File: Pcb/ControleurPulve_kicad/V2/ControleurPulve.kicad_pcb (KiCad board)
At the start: 2 copper layers, 92 parts, among them J1 Screw_Terminal_01x02, J10 Screw_Terminal_01x04, J11 Screw_Terminal_01x04, J12 Conn_01x03_Pin, J13 Conn_01x03_Pin, J14 Conn_01x03_Pin, J15 Conn_01x03_Pin, J16 Screw_Terminal_01x04, J17 Screw_Terminal_01x04, J18 Conn_01x03_Pin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

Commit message: PCB : silkscreen et placement (non routé)
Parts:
- added H5: e, MountingHole:MountingHole_3.2mm_M3, F.Cu at (131.1, 67.1)
- added H6: e, MountingHole:MountingHole_3.2mm_M3, F.Cu at (163.2, 88.4)
- added H7: e, MountingHole:MountingHole_3.2mm_M3, F.Cu at (131.1, 88.4)
- added R23: 2k5, Resistor_SMD:R_0603_1608Metric, F.Cu at (112.4, 88.6)
- added U9: ~, DIY_Modules:GY-NEO6MV2_25_36, F.Cu at (147.2, 77.7)
- G*** (x3): moved to B.Cu
- H4: value ~ -> e; footprint MountingHole:MountingHole_4.3mm_M4_DIN965_Pad_TopBottom -> MountingHole:MountingHole_3.2mm_M3
- J1: footprint TerminalBlock_RND:TerminalBlock_RND_205-00287_1x02_P5.08mm_Horizontal -> TerminalBlock_Phoenix:TerminalBlock_Phoenix_MKDS-1,5-2-5.08_1x02_P5.08mm_Horizontal
- J7: footprint Connector_PinSocket_2.54mm:PinSocket_1x06_P2.54mm_Vertical -> Connector_JST:JST_XH_B6B-XH-A_1x06_P2.50mm_Vertical
- R4: footprint Resistor_SMD:R_1206_3216Metric -> Resistor_SMD:R_0805_2012Metric
- moved G*** 269.1 mm to (180.8, 104.6), turned to 180 degrees
- moved G*** 225.5 mm to (151.6, 104.6), turned to 180 degrees
- moved TP3 185.4 mm to (105.5, 49.7)
- moved TP4 185.4 mm to (105.5, 53.2)
- moved TP5 185.4 mm to (105.5, 56.6)
- moved G*** 180.9 mm to (117.9, 104.1), turned to 180 degrees
- moved H1 168.4 mm to (91.0, 95.0)
- moved H4 118.7 mm to (163.2, 67.1)
- moved H3 108.0 mm to (170.0, 80.0)
- moved C4 86.6 mm to (112.2, 72.0)
- moved U1 81.8 mm to (120.5, 84.1)
- moved R1 80.3 mm to (139.6, 87.0), turned to -90 degrees
- moved R3 80.3 mm to (112.3, 86.6), turned to 180 degrees
- moved H2 79.0 mm to (191.0, 95.0)
- moved R2 74.5 mm to (137.0, 87.0), turned to -90 degrees
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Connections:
- J19 pad 2: Net-(J19-Pin_1) -> Net-(J19-Pin_2)
- J19 pad 3: Net-(J19-Pin_1) -> Net-(J19-Pin_3)
- JP5 pad 1: GND -> Net-(JP5-A)
- JP7 pad 1: GND -> Net-(JP5-A)
- R18 pad 1: Net-(J19-Pin_1) -> Net-(J19-Pin_2)
- R22 pad 2: Net-(J19-Pin_1) -> Net-(J19-Pin_3)
- U3 pad 3: unconnected-(U3-DEN-Pad3) -> Net-(U3-DEN)
- U4 pad 1: GND -> Net-(JP5-A)
- U8 pad 2: Net-(J19-Pin_1) -> Net-(J19-Pin_2)
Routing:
- added copper zone on B.Cu, net (none)
- added copper zone on F.Cu, net (none)
- added copper zone on In2.Cu, net (none)
- removed copper zone on B.Cu, net GND
- removed copper zone on F.Cu, net GND
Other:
- board outline added: 111.8 x 59.1 mm
- copper layers 2 -> 4
- board text added: "0-3V3"
- board text added: "0x49"
- board text added: "0x4A"
- board text added: "2025-10"
- board text added: "4-20 mA"
- board text added: "Ana"
- board text added: "Cl"
- board text added: "DG"
- board text added: "DM1-G"
- board text added: "DM2-cG"
- board text added: "DM3-cD"
- board text added: "DM4-D"
- board text added: "Da"
- board text added: "Débitdouille V2.0"
- board text added: "ESP32-C6 Xiao supermini"
- board text added: "Freq"
- board text added: "Gnd"
- board text added: "PRESS."
- board text added: "PWR"
- board text added: "Rx"
- board text added: "S"
- board text added: "Tx"
- board text added: "Vcc"
- board text added: "bypass 12Vout"
- board text added: "debit 4-20"
- board text added: "npn"
- board text added: "pnp"
- board text added: "press."
- board text removed: "DATA"
- board text removed: "Débitdouille V1.0"
- board text removed: "ESP32"
- board text removed: "PRESSION"
- board text removed: "RXD"
- board text removed: "TXD"

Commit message: Mise en prod
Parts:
- added D5: red, LED_SMD:LED_0603_1608Metric_Pad1.05x0.95mm_HandSolder, F.Cu at (109.0, 66.3)
- added FID1: Fiducial, Fiducial:Fiducial_0.5mm_Mask1.5mm, F.Cu at (87.0, 122.0)
- added FID2: Fiducial, Fiducial:Fiducial_0.5mm_Mask1.5mm, F.Cu at (195.0, 122.0)
- added FID3: Fiducial, Fiducial:Fiducial_0.5mm_Mask1.5mm, F.Cu at (87.0, 67.0)
- added G***: LOGO, LOGO, B.Cu at (93.2, 104.5)
- added R24: 2.2k, Resistor_SMD:R_0603_1608Metric_Pad0.98x0.95mm_HandSolder, F.Cu at (109.5, 68.9)
- C3: value 10uF -> 10uF X5R
- C5: value C -> 100nF
- C6: value C -> 10uF X5R
- C8: footprint Capacitor_SMD:C_0805_2012Metric -> Capacitor_SMD:C_0603_1608Metric
- D3: value LED -> green
- D4: value LED -> blue
- H1, H2, H3: footprint MountingHole:MountingHole_4.3mm_M4_DIN965_Pad_TopBottom -> MountingHole:MountingHole_3.2mm_M3_DIN965_Pad
- JP1: footprint Jumper:SolderJumper-2_P1.3mm_Open_TrianglePad1.0x1.5mm -> Jumper:SolderJumper-2_P1.3mm_Open_RoundedPad1.0x1.5mm; moved to B.Cu
- JP2, JP4, JP5, JP6, JP7: moved to B.Cu
- R4: value 150R .5% -> 150R .1%
- U5, U6, U7, U8: footprint Package_DIP:DIP-4_W7.62mm_SMDSocket_SmallPads -> Package_DIP:DIP-4_W8.89mm_SMDSocket_LongPads
- moved TP3 104.2 mm to (194.1, 104.7)
- moved TP4 98.1 mm to (191.2, 101.1)
- moved TP5 75.3 mm to (177.6, 78.5)
- moved R1 12.1 mm to (131.1, 95.5), turned to 90 degrees
- moved C3 10.8 mm to (112.4, 93.6), turned to 90 degrees
- moved JP1 9.42 mm to (110.2, 96.5)
- moved R2 9.20 mm to (133.6, 95.5), turned to 90 degrees
- moved H3 3.80 mm to (170.0, 76.2)
- moved JP4 3.27 mm to (122.7, 74.0), turned to 0 degrees
- moved R14 3.27 mm to (111.3, 68.9), turned to 90 degrees
- moved C11 3.02 mm to (172.7, 83.2)
- moved C10 2.39 mm to (172.7, 87.6)
- moved C9 2.39 mm to (172.7, 85.7)
- moved R23 2.34 mm to (112.4, 86.3)
- moved G*** 1.93 mm to (182.8, 104.8)
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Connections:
- U2 pad 1: unconnected-(U2-GPIO0/A0/D0-Pad1) -> ESP_LED
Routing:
- net SDA: track 0.00 -> 125.7 mm, vias 0 -> 2
- net SCL: track 0.00 -> 119.4 mm, vias 0 -> 3
- net debit_centre_droit: track 0.00 -> 111.4 mm, vias 0 -> 2
- net debit_droit: track 0.00 -> 110.1 mm, vias 0 -> 1
- net pression: track 0.00 -> 102.9 mm
- net debit_centre_gauche: track 0.00 -> 90.0 mm, vias 0 -> 2
- net 12V_OUT: track 0.00 -> 84.6 mm, vias 0 -> 5
- net 3V3_OUT: track 0.00 -> 76.8 mm, vias 0 -> 9
- net debit2_4-20: track 0.00 -> 62.8 mm, vias 0 -> 3
- net debit_gauche: track 0.00 -> 53.7 mm, vias 0 -> 2
- net debit1_4-20: track 0.00 -> 52.8 mm, vias 0 -> 1
- net debit3_4-20: track 0.00 -> 41.4 mm, vias 0 -> 1
- net 12V: track 0.00 -> 41.2 mm, vias 0 -> 1
- net pwr_12V_out: track 0.00 -> 39.2 mm, vias 0 -> 2
- net debit4_4-20: track 0.00 -> 39.0 mm, vias 0 -> 1
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- added copper zone on In1.Cu, net 12V_OUT
- added copper zone on In1.Cu, net 3V3_OUT
- added copper zone on In1.Cu, net 5V
- added copper zone on B.Cu, net GND
- added copper zone on F.Cu, net GND
- added copper zone on In2.Cu, net GND
- removed copper zone on B.Cu, net (none)
- removed copper zone on F.Cu, net (none)
- removed copper zone on In2.Cu, net (none)
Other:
- board text added: "12Vo"
- board text added: "ADC Mux sélection"
- board text added: "DEBITDOUILLE V2.0"
- board text added: "GPS pwr"
- board text added: "Pbm"
- board text added: "Xiao ESP32-C3/C6"
- board text removed: "ESP32-C6 Xiao supermini"

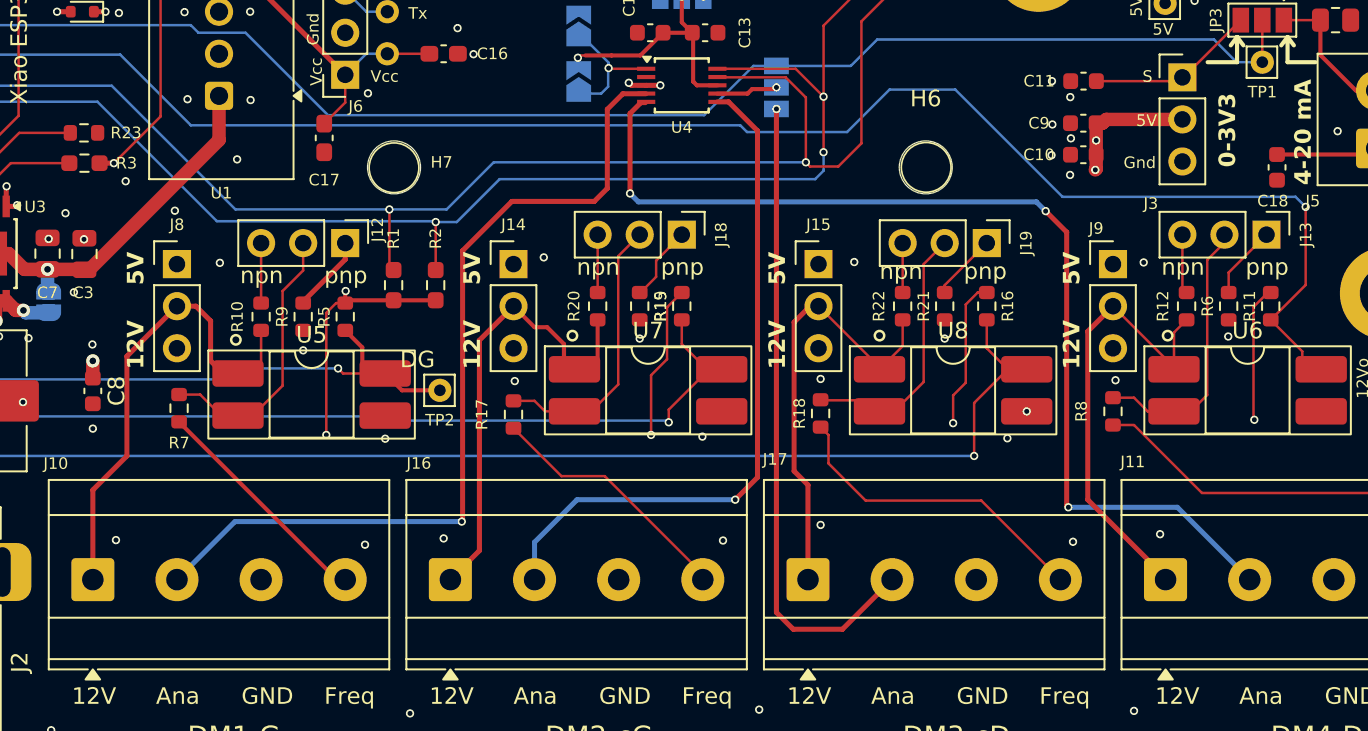
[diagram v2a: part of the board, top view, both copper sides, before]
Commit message: Dév PCB : en cours de validation PCB reçus Code V2
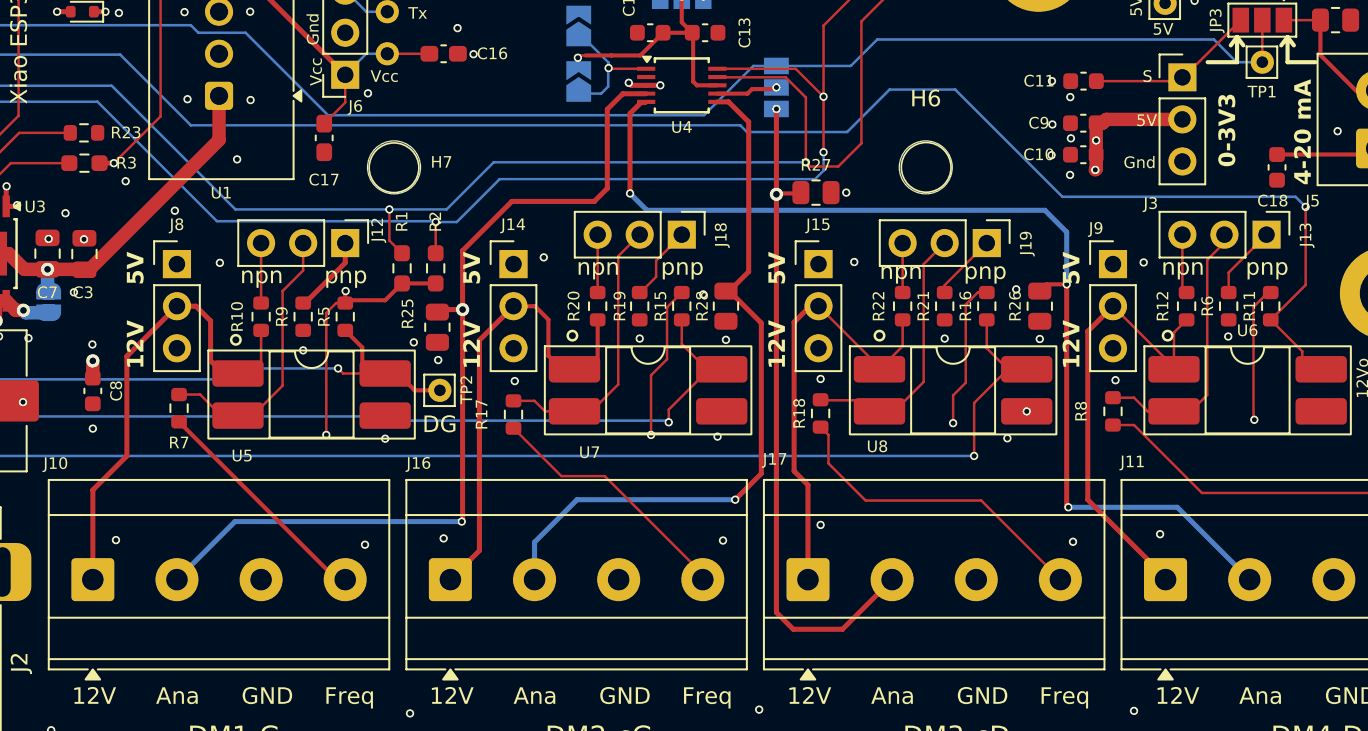
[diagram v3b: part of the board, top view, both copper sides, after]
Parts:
- added R25: 150R .1%, Resistor_SMD:R_0805_2012Metric, F.Cu at (133.7, 98.0)
- added R26: 150R .1%, Resistor_SMD:R_0805_2012Metric, F.Cu at (170.1, 96.8)
- added R27: 150R .1%, Resistor_SMD:R_0805_2012Metric, F.Cu at (156.6, 89.9)
- added R28: 150R .1%, Resistor_SMD:R_0805_2012Metric, F.Cu at (151.1, 96.8)
- moved R1 1.14 mm to (131.6, 94.5)
- moved R2 1.02 mm to (133.6, 94.5)
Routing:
- net debit2_4-20: track 62.8 -> 64.6 mm
- net debit4_4-20: track 39.0 -> 40.6 mm, vias 1 -> 2
- net debit1_4-20: track 52.8 -> 54.4 mm, vias 1 -> 2
- net debit3_4-20: track 41.4 -> 43.0 mm
- net SCL: track 119.4 -> 118.4 mm
- net SDA: track 125.7 -> 124.9 mm
- net Net-(J14-Pin_2): track 28.3 -> 29.0 mm
- net 3V3_OUT: track 76.8 -> 77.3 mm
- net GND: vias 102 -> 109
